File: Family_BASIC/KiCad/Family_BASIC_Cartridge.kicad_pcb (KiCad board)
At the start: 2 copper layers, 93 x 79.5 mm, 19 parts, among them IC1 Working RAM (62256), IC2 PRG ROM (27256), IC3 74HCT20, IC4 CHR ROM (27C64), SW1 BACKUP SW, SW2 RAM BANK SW

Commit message: PCB design continues
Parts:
- moved C1 27.1 mm to (140.7, 111.4), turned to 90 degrees
- moved C2 3.73 mm to (110.2, 127.9)
- moved IC4 3.73 mm to (114.0, 131.7)
- moved C3 3.73 mm to (110.2, 112.7)
- moved IC3 3.73 mm to (129.2, 105.1)
- moved SW2 2.60 mm to (120.8, 94.1)
- moved BT1 2.08 mm to (101.3, 77.9)
- moved C4 1.65 mm to (59.4, 103.7)
- moved C5 1.65 mm to (59.4, 127.9)
- moved IC1 1.65 mm to (63.2, 107.6)
- moved IC2 1.65 mm to (63.2, 131.7)
- moved R2 1.65 mm to (63.2, 111.4)
- moved BT2 1.10 mm to (133.0, 77.9)
- moved R3 0.47 mm to (75.9, 87.3)
- moved D2 0.47 mm to (63.2, 79.7)
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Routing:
- net /V_{CC}: track 0.00 -> 83.9 mm
- net /PA_{10}: track 0.00 -> 60.0 mm, vias 0 -> 4
- net /D_{0}: track 0.00 -> 40.1 mm
- net /D_{1}: track 0.00 -> 34.6 mm
- net /RAM_{~{CS}}: track 0.00 -> 31.6 mm
- net /PD_{3}: track 0.00 -> 31.1 mm
- net /PD_{7}: track 0.00 -> 29.0 mm
- net /PD_{6}: track 0.00 -> 29.0 mm
- net /PA_{11}: track 0.00 -> 29.0 mm, vias 0 -> 2
- net /PD_{5}: track 0.00 -> 29.0 mm
- net /PA_{9}: track 0.00 -> 29.0 mm, vias 0 -> 2
- net /PD_{4}: track 0.00 -> 28.9 mm
- net /PA_{13}: track 0.00 -> 27.8 mm
- net /A_{6}: track 15.9 -> 42.0 mm
- net /A_{3}: track 15.7 -> 41.7 mm
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
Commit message: Update Family_BASIC_Cartridge.kicad_pcb
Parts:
- moved C1 6.39 mm to (139.5, 105.1), turned to -90 degrees
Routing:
- net /V_{CC}: track 83.9 -> 244.3 mm
- net Net-(SW1-B): track 0.00 -> 101.1 mm, vias 0 -> 1
- net /A_{14}: track 0.00 -> 98.1 mm, vias 0 -> 1
- net /O2: track 0.00 -> 93.9 mm, vias 0 -> 2
- net /A_{13}: track 0.00 -> 92.4 mm
- net /~{ROMSEL}: track 0.00 -> 89.1 mm, vias 0 -> 1
- net /SWA_{14}: track 3.81 -> 59.4 mm
- net Net-(BT1--): track 0.00 -> 52.5 mm
- net Net-(BT1-+): track 0.00 -> 51.8 mm
- net /SWA_{13}: track 0.00 -> 48.9 mm
- net /~{RD}: track 0.00 -> 43.0 mm
- net /A_{11}: track 25.0 -> 65.7 mm, vias 0 -> 1
- net /A_{10}: track 25.0 -> 65.4 mm, vias 0 -> 1
- net /D_{4}: track 25.0 -> 63.9 mm, vias 0 -> 1
- net /D_{5}: track 25.0 -> 61.6 mm, vias 0 -> 2
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- added copper zone on B.Cu, net /GND
- added copper zone on F.Cu, net /GND

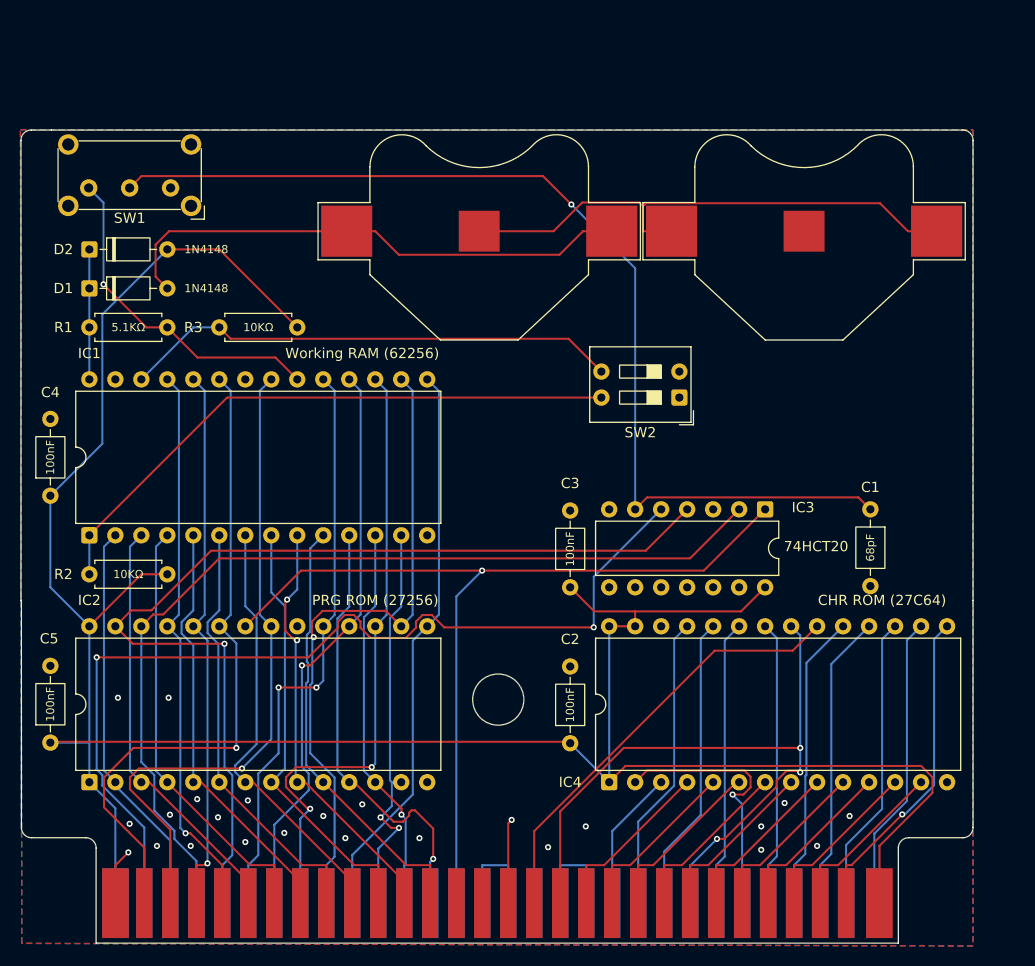
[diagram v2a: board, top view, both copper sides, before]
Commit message: Initial PCB layout completed
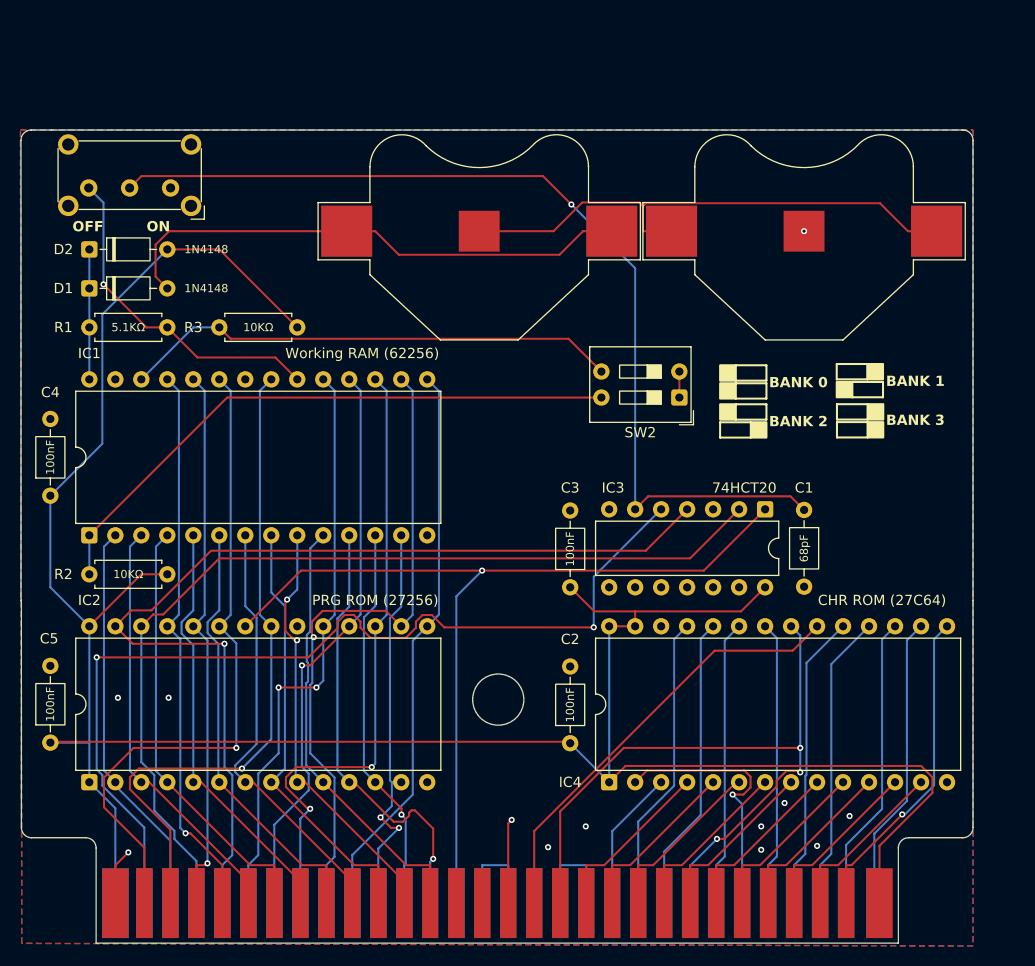
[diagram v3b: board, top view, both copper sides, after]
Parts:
- moved C1 6.48 mm to (133.0, 105.1)
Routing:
- net Net-(SW1-B): track 101.1 -> 94.8 mm
- net /GND: track 13.8 -> 16.3 mm, vias 24 -> 12
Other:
- board text added: "BANK 0"
- board text added: "BANK 1"
- board text added: "BANK 2"
- board text added: "BANK 3"
- board text added: "OFF"
- board text added: "ON"

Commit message: Additional silkscreen text
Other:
- board text added: "Nintendo Family BASIC"
- board text added: "Nintendo Family BASIC, Rev. A Brett Hallen, Dec 2025"
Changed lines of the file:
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@@
 	)
 	(gr_rect
-		(start 140.765 98.044389)
-		(end 139.265 96.544389)
-		(stroke
-			(width 0.2)
-			(type solid)
-		)
-		(fill yes)
-		(layer "F.SilkS")
-	)
-	(gr_rect
-		(start 129.347 98.056389)
-		(end 127.847 96.556389)
+		(start 139.265 96.544389)
+		(end 140.765 98.044389)
+		(stroke
+			(width 0.2)
+			(type solid)
+		)
+		(fill yes)
+		(layer "F.SilkS")
+	)
+	(gr_rect
+		(start 127.847 96.556389)
+		(end 129.347 98.056389)
 		(stroke
 			(width 0.2)
@@
 	)
 	(gr_rect
-		(start 140.741 92.365389)
-		(end 139.241 90.865389)
+		(start 139.241 90.865389)
+		(end 140.741 92.365389)
 		(stroke
 			(width 0.2)
@@
 	)
 	(gr_rect
-		(start 139.241 96.290389)
-		(end 136.241 94.790389)
-		(stroke
-			(width 0.2)
-			(type solid)
-		)
-		(fill no)
-		(layer "F.SilkS")
-	)
-	(gr_rect
-		(start 140.765 96.290389)
-		(end 139.265 94.790389)
+		(start 136.241 94.790389)
+		(end 139.241 96.290389)
+		(stroke
+			(width 0.2)
+			(type solid)
+		)
+		(fill no)
+		(layer "F.SilkS")
+	)
+	(gr_rect
+		(start 139.265 94.790389)
+		(end 140.765 96.290389)
 		(stroke
 			(width 0.2)
@@
 	)
 	(gr_rect
-		(start 127.823 98.056389)
-		(end 124.823 96.556389)
+		(start 124.823 96.556389)
+		(end 127.823 98.056389)
 		(stroke
 			(width 0.2)
@@
 	)
 	(gr_rect
-		(start 139.217 92.365389)
-		(end 136.217 90.865389)
-		(stroke
-			(width 0.2)
-			(type solid)
-		)
-		(fill no)
-		(layer "F.SilkS")
-	)
-	(gr_rect
-		(start 139.241 98.044389)
-		(end 136.241 96.544389)
+		(start 136.217 90.865389)
+		(end 139.217 92.365389)
+		(stroke
+			(width 0.2)
+			(type solid)
+		)
+		(fill no)
+		(layer "F.SilkS")
+	)
+	(gr_rect
+		(start 136.241 96.544389)
+		(end 139.241 98.044389)
 		(stroke
 			(width 0.2)
@@
 		(layer "Edge.Cuts")
 	)
+	(gr_text "Nintendo Family BASIC"
+		(at 111.567 101.636389 0)
+		(layer "F.SilkS")
+		(effects
+			(font
+				(size 2 2)
+				(thickness 0.25)
+			)
+			(justify left bottom)
+		)
+	)
 	(gr_text "OFF"
 		(at 61.529 78.014389 0)
@@
 		)
 	)
+	(gr_text "Nintendo Family BASIC, Rev. A\nBrett Hallen, Dec 2025"
+		(at 147.127 87.920389 0)
+		(layer "B.SilkS")
+		(effects
+			(font
+				(size 1 1)
+				(thickness 0.1)
+			)
+			(justify left bottom mirror)
+		)
+	)

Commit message: Finalised initial Rev. A design
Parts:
- added JP1: A_{12} Enable, Jumper:SolderJumper-3_P1.3mm_Bridged12_RoundedPad1.0x1.5mm, B.Cu at (66.1, 110.1)
- moved R2 28.9 mm to (77.8, 86.5), turned to 180 degrees
- moved SW1 12.8 mm to (78.6, 63.3)
- moved D1 11.0 mm to (70.2, 75.1)
- moved R1 11.0 mm to (70.2, 78.9)
- moved BT1 10.0 mm to (98.7, 68.2)
- moved D2 10.0 mm to (70.2, 72.5)
- moved BT2 9.86 mm to (131.4, 68.2)
- moved C3 7.79 mm to (107.0, 105.6)
- moved IC3 7.79 mm to (126.1, 97.9)
- moved C1 7.79 mm to (129.9, 98.0)
- moved SW2 6.80 mm to (118.5, 87.8)
- moved R3 4.99 mm to (77.8, 82.7), turned to 180 degrees
- moved IC4 3.23 mm to (110.8, 131.0)
- moved C2 3.23 mm to (107.0, 127.1)
- moved C4 2.83 mm to (61.3, 101.7)
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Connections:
- net /SWA_{13} renamed /A_{13}SW
- net /SWA_{14} renamed /A_{14}SW
- H1 pad 14: /R/_{W} -> /R/~{W}
- IC1 pad 2: /A_{12} -> /A_{12}EN
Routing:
- net /GND: track 16.3 -> 377.9 mm, vias 12 -> 19
- net /R/~{W}: track 0.00 -> 83.9 mm, vias 0 -> 2
- net Net-(SW1-B): track 94.8 -> 83.4 mm
- net Net-(BT1-+): track 51.8 -> 40.5 mm
- net /V_{CC}: track 244.3 -> 236.1 mm
- net /O2: track 93.9 -> 86.3 mm, vias 2 -> 1
- net /RAMV_{CC}: track 12.7 -> 19.9 mm
- net /PA_{10}: track 68.3 -> 74.3 mm, vias 3 -> 1
- net /PA_{12}: track 26.1 -> 31.3 mm
- net /A_{12}EN: track 0.00 -> 5.20 mm
- net /A_{13}SW: track 48.9 -> 44.8 mm
- net /D_{6}: track 56.2 -> 60.1 mm, vias 1 -> 0
- net /D_{3}: track 55.2 -> 59.0 mm, vias 0 -> 1
- net /A_{11}: track 65.7 -> 62.1 mm
- net /A_{12}: track 39.1 -> 35.7 mm
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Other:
- board size 93 x 79.5 mm -> 90 x 90 mm
- board text added: "Nintendo Family BASIC 8KB"
- board text removed: "Nintendo Family BASIC"

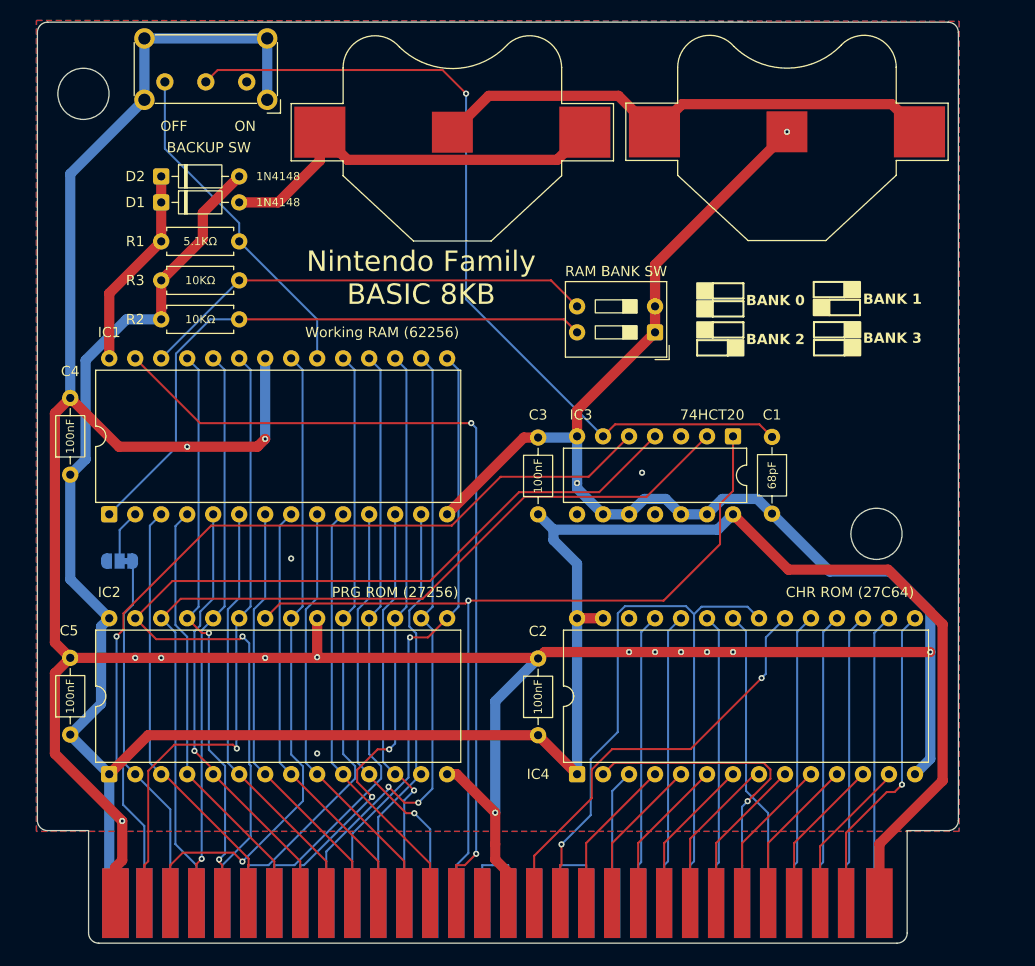
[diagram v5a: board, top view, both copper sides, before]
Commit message: Minor cosmetic PCB changes
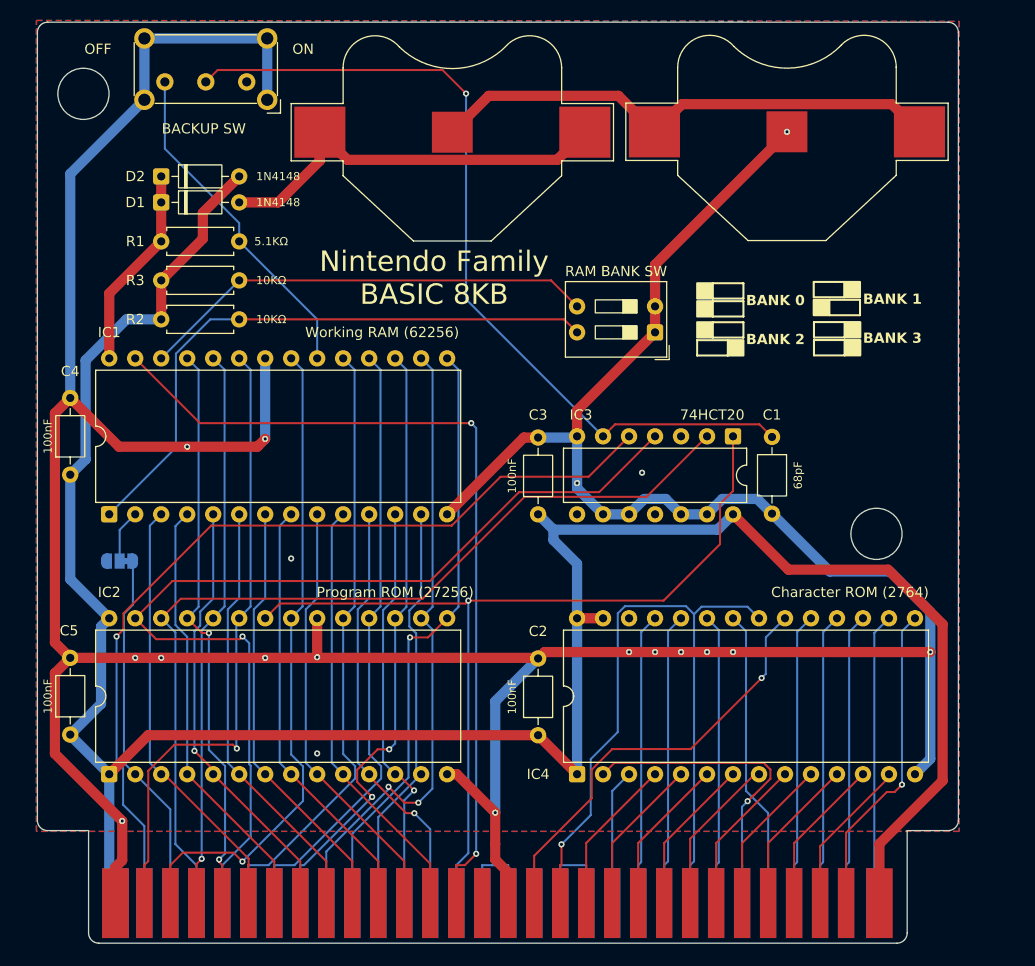
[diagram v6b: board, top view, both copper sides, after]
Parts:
- H1: value Famicom_Cartridge_Edge -> Famicom Cartridge Edge
- IC2: value PRG ROM (27256) -> Program ROM (27256)
- IC4: value CHR ROM (27C64) -> Character ROM (2764)
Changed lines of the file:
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@@
 		)
 		(property "Value" "100nF"
-			(at 3.75 0 90)
+			(at 3.740367 -2.189132 90)
 			(layer "F.SilkS")
 			(effects
@@
 			)
 		)
-		(property "Value" "CHR ROM (27C64)"
+		(property "Value" "Character ROM (2764)"
 			(at 17.78 26.67 180)
 			(layer "F.SilkS")
@@
 		)
 		(property "Value" "BACKUP SW"
-			(at 3.7075 -6.4175 0)
+			(at 4.198062 -4.57819 0)
 			(layer "F.SilkS")
 			(effects
@@
 		)
 		(property "Value" "100nF"
-			(at 3.75 0 90)
+			(at 3.75 -2.189132 90)
 			(layer "F.SilkS")
 			(effects
@@
 		)
 		(property "Value" "100nF"
-			(at 3.75 0 90)
+			(at 3.75 -2.54 90)
 			(layer "F.SilkS")
 			(effects
@@
 			)
 		)
-		(property "Value" "Famicom_Cartridge_Edge"
+		(property "Value" "Famicom Cartridge Edge"
 			(at 12.93 -0.58 0)
 			(unlocked yes)
@@
 			)
 		)
-		(property "Value" "PRG ROM (27256)"
+		(property "Value" "Program ROM (27256)"
 			(at 17.78 27.94 180)
 			(layer "F.SilkS")
@@
 		)
 		(property "Value" "10KΩ"
-			(at 3.81 0 0)
+			(at -3.124491 0 0)
 			(layer "F.SilkS")
 			(effects
@@
 		)
 		(property "Value" "68pF"
-			(at 3.75 0 90)
+			(at 3.75 -2.54 90)
 			(layer "F.SilkS")
 			(effects
@@
 		)
 		(property "Value" "10KΩ"
-			(at 3.81 0 0)
+			(at -3.124491 0 0)
 			(layer "F.SilkS")
 			(effects
@@
 		)
 		(property "Value" "5.1KΩ"
-			(at 3.81 0 0)
+			(at 10.744491 0 0)
 			(layer "F.SilkS")
 			(effects
@@
 		)
 		(property "Value" "100nF"
-			(at 3.75 0 90)
+			(at 3.75 -2.54 90)
 			(layer "F.SilkS")
 			(effects
@@
 	)
 	(gr_text "Nintendo Family \nBASIC 8KB"
-		(at 95.604 85.2322 0)
+		(at 96.874 85.2322 0)
 		(layer "F.SilkS")
 		(effects
@@
 	)
 	(gr_text "OFF"
-		(at 70.115 68.2122 0)
+		(at 62.692568 60.675853 0)
 		(layer "F.SilkS")
 		(effects
@@
 	)
 	(gr_text "ON"
-		(at 77.354 68.2122 0)
+		(at 83.019334 60.675853 0)
 		(layer "F.SilkS")
 		(effects

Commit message: Only one button cell holder needed
Each CR2032 button cell is 3V, duh, so only one needed to replace the 2xAA cells.
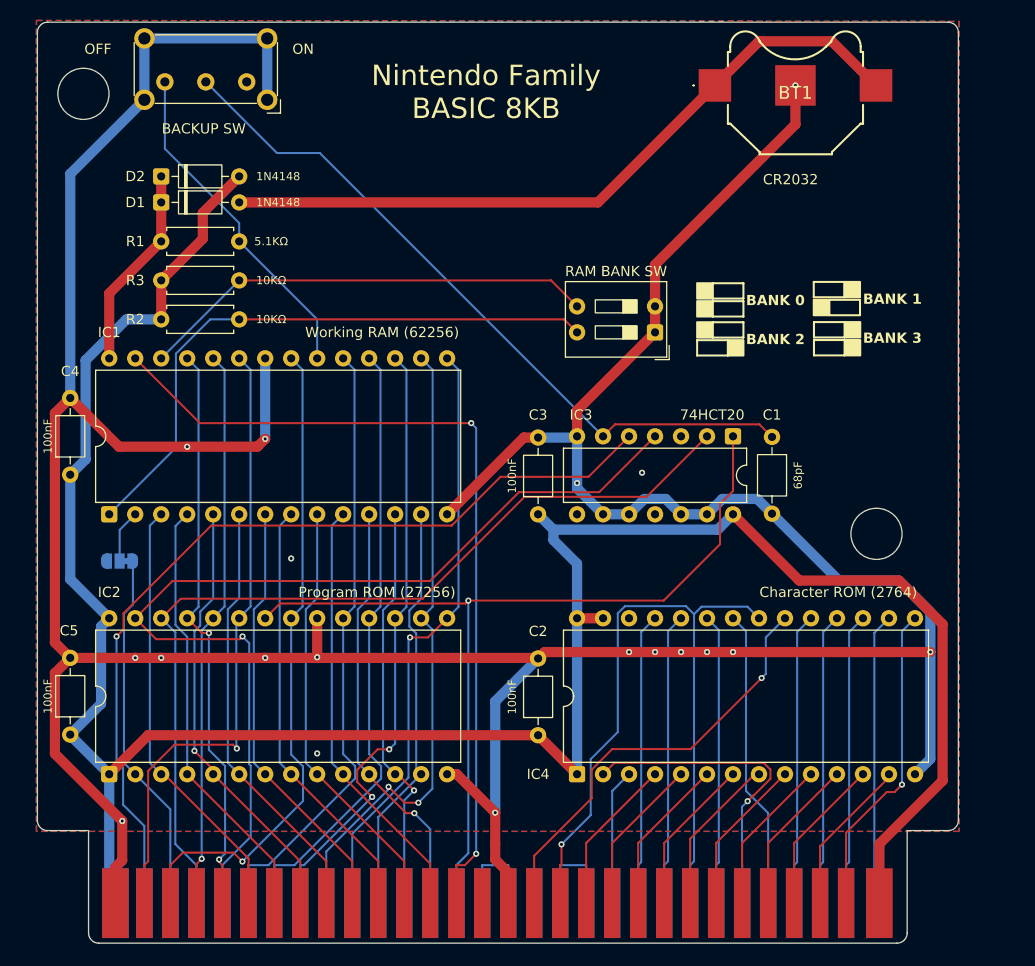
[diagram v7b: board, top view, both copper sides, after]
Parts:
- removed BT2: 1.5V, Battery:BatteryHolder_Multicomp_BC-2001_1x2032
- BT1: value 1.5V -> 3V; footprint Battery:BatteryHolder_Multicomp_BC-2001_1x2032 -> Clueless_Engineer:3000
- moved BT1 33.8 mm to (132.2, 64.4)
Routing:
- net Net-(BT1--): track 50.8 -> 0.00 mm
- net Net-(BT1-+): track 40.5 -> 70.5 mm
- net Net-(SW1-B): track 83.4 -> 70.7 mm, vias 1 -> 0
- net /GND: track 377.9 -> 382.8 mm
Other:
- board text added: "CR2032"
